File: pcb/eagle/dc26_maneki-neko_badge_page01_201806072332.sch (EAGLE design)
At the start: 49 parts, among them IC1 STM32F030C8T, T1 RK7002BMT116, U2 ESP01, X1 22-23-2021, X2 22-23-2031

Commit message: board outline in, some minor edits to schematic, board ready for component placement
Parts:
- removed LED1, LED2: WS2812B5050, adafruit_2015:WS2812B5050
- removed U$5: PAM2301CAAB330, PAM2301CAAB120:PAM2301CAAB330
- added C10: 1uF/16V/X7R, rcl:C-USC0805
- added H3: TSW-102-07-G-D, con-samtec:TSW-102-07-G-D
- added R26, R27, R28: 10k/5%, rcl:R-US_R0805
- added R29: NO POP, rcl:R-US_R0805
- added U3: ESP01, esp8266modules:ESP01
- C1: value SHORT -> 10uF/16V/X5R
- C3: value 10uF/16V/X5R -> SHORT
- R25: value 10k/5% -> 1k/5%
- U2: value ESP01 -> PAM2301CAAB330; device esp8266modules:ESP01 -> PAM2301CAAB120:PAM2301CAAB330
- U5, U6: value (none) -> MIC2005A-1YM5-TR
- renumbered IC1 to U1, U$1 to D1, U$13 to H1, U$2 to D2, U$3 to U6, U$4 to U5, U$6 to U4, X2 to H2
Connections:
- removed net VCC: C4.1, C5.1, C6.1, H1.1, R21.2, R22.2, U5.VIN, U6.VIN
- new net BOOT0: R28.2, R29.1, U1MCU.BOOT0
- new net I2C1_SCL: H3-4.1, R26.1, U1MCU.PF6
- new net I2C1_SDA: H3-3.1, R27.1, U1MCU.PF7
- net !RESET: now also U1MCU.NRST
- net 3V3: now also C10.1, C2.1, C4.1, C5.1, C6.1, H1.1, H3-1.1, R21.2, R22.2, R26.2, R27.2, R29.2, U1MCU.VDDA, U5.VIN, U6.VIN; no longer C1.1
- net ESP-CH_PD: now also U3.CH_PD; no longer U2.CH_PD
- net ESP-GPIO0: now also U3.GPIO0; no longer U2.GPIO0
- net ESP-GPIO2: now also U3.GPIO2; no longer U2.GPIO2
- net ESP-RST: now also U3.RST; no longer U2.RST
- net ESP-RXD: now also U3.RXD; no longer U2.RXD
- net ESP-TXD: now also U3.TXD; no longer U2.TXD
- net GND: now also C1.2, C10.2, H3-2.1, R28.1, U1MCU.VSSA, U3.GND; no longer C3.2, U$5.GND
- net LED-SEG-A: now also R18.2; no longer R19.2
- net LED-SEG-B: now also R19.2; no longer R18.2
- net LED-SEG-C: now also R15.2; no longer R17.2
- net LED-SEG-E: now also R17.2; no longer R15.2
- net LED-SEG-F: now also R12.2; no longer R14.2
- net LED-SEG-H: now also R14.2; no longer R12.2
- net N$1: now also U2.SW; no longer U$5.SW
- net N$2: now also U2.EN; no longer U$5.EN
- net N$3: now also C3.2, U2.VOUT/FB; no longer C1.2, U$5.VOUT/FB
- net PB0: now also R18.1; no longer R19.1
- net PB1: now also R19.1; no longer R18.1
- net PB2: now also R15.1; no longer R17.1
- net PB4: now also R17.1; no longer R15.1
- net PB5: now also R12.1; no longer R14.1
- net PB7: now also R14.1; no longer R12.1
- net VBAT: now also C1.1, U2.VIN; no longer C2.1, U$5.VIN
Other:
- note added: "BADGELIFE SHITTY ADD-ON HEADER"
- note added: "VOLTAGE REGULATOR"
- moved on the sheet: C1, C2, C3, R10, R12, R14, R15, R16, R17, R18, R19, R20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

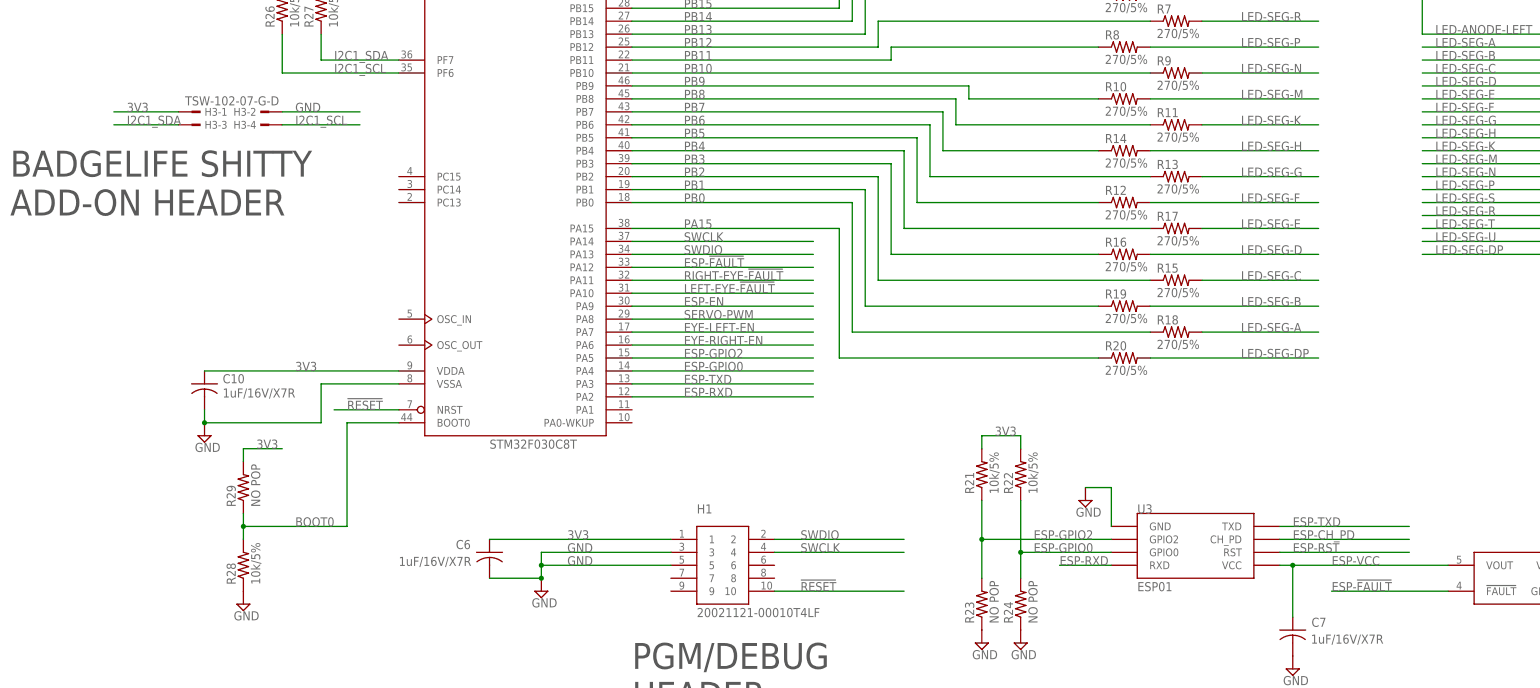
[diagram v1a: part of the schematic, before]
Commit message: more layout. changed out connectors to support a clean 'art' (top) side. shooting for 2 layers, might need to be 4 to avoid a ton of routing time.
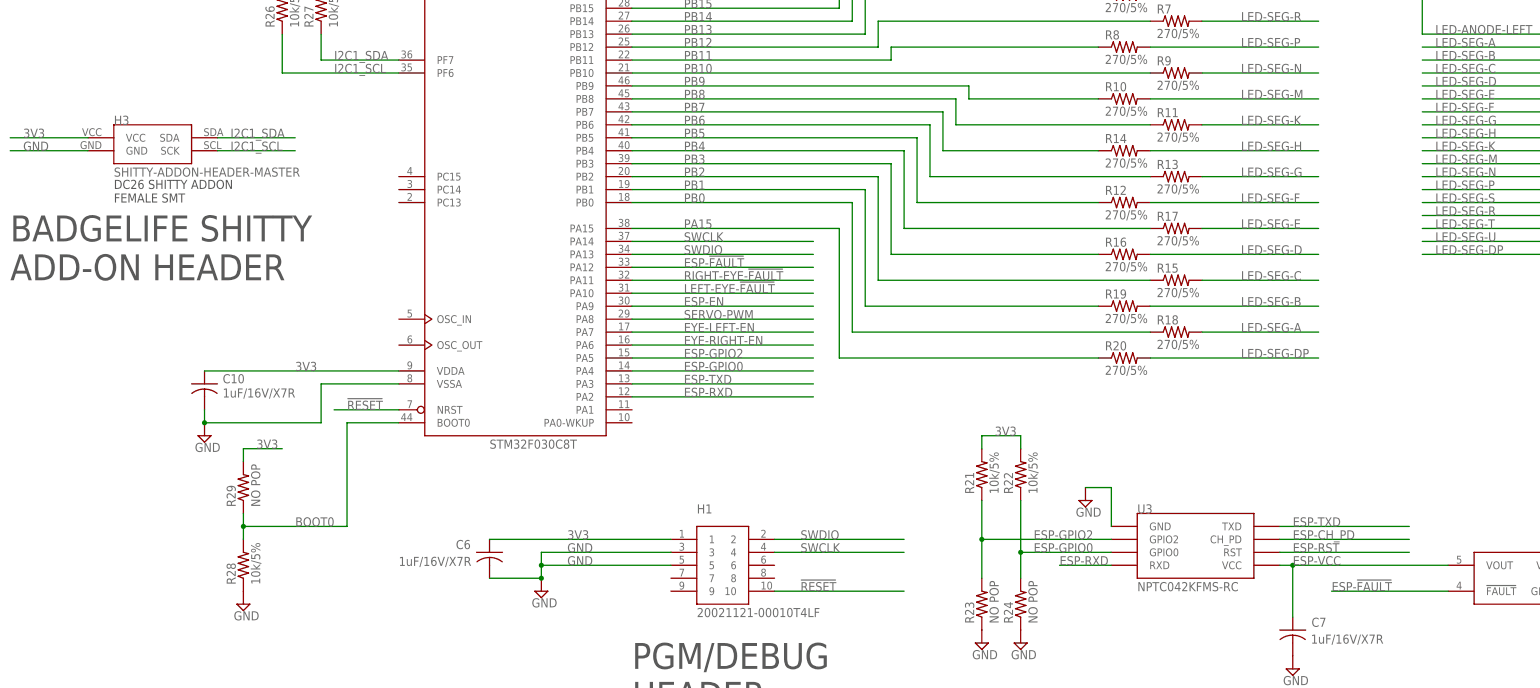
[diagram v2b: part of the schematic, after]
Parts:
- H3: value TSW-102-07-G-D -> SHITTY-ADDON-HEADER-MASTER; device con-samtec:TSW-102-07-G-D -> dc26-shitty-addon:SHITTY-ADDON-HEADER-MASTER
- U3: value ESP01 -> NPTC042KFMS-RC; device esp8266modules:ESP01 -> NPTC042KFMS-RC:NPTC042KFMS-RC
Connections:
- net 3V3: now also H3.VCC; no longer H3-1.1
- net ESP-VCC: now also U3.VCC
- net GND: now also H3.GND; no longer H3-2.1
- net I2C1_SCL: now also H3.SCK; no longer H3-4.1
- net I2C1_SDA: now also H3.SDA; no longer H3-3.1
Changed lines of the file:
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@@
 </classes>
 <parts>
-<part name="U3" library="esp8266modules" deviceset="ESP01" device=""/>
 <part name="U1" library="micro-stm_v3" deviceset="STM32F030C*T" device="" technology="8"/>
 <part name="X1" library="con-molex" library_urn="urn:adsk.eagle:library:165" deviceset="22-23-2021" device=""/>
@@
 <part name="C10" library="rcl" library_urn="urn:adsk.eagle:library:334" deviceset="C-US" device="C0805" package3d_urn="urn:adsk.eagle:package:23617/2" value="1uF/16V/X7R"/>
 <part name="SUPPLY17" library="supply2" library_urn="urn:adsk.eagle:library:372" deviceset="GND" device=""/>
-<part name="H3" library="con-samtec" library_urn="urn:adsk.eagle:library:184" deviceset="TSW-102-*-G" device="-D" technology="07"/>
 <part name="R29" library="rcl" library_urn="urn:adsk.eagle:library:334" deviceset="R-US_" device="R0805" package3d_urn="urn:adsk.eagle:package:23553/2" value="NO POP"/>
 <part name="R28" library="rcl" library_urn="urn:adsk.eagle:library:334" deviceset="R-US_" device="R0805" package3d_urn="urn:adsk.eagle:package:23553/2" value="10k/5%"/>
 <part name="SUPPLY18" library="supply2" library_urn="urn:adsk.eagle:library:372" deviceset="GND" device=""/>
+<part name="H3" library="dc26-shitty-addon" deviceset="SHITTY-ADDON-HEADER-MASTER" device=""/>
+<part name="U3" library="NPTC042KFMS-RC" deviceset="NPTC042KFMS-RC" device=""/>
 </parts>
 <sheets>
@@
 <text x="-121.92" y="40.64" size="5.08" layer="97">PGM/DEBUG
 HEADER</text>
-<text x="-243.84" y="137.16" size="5.08" layer="97">BADGELIFE SHITTY
+<text x="-243.84" y="124.46" size="5.08" layer="97">BADGELIFE SHITTY
 ADD-ON HEADER</text>
 <text x="-134.62" y="238.76" size="5.08" layer="97">VOLTAGE
@@
 </plain>
 <instances>
-<instance part="U3" gate="G$1" x="-10.16" y="68.58"/>
 <instance part="U1" gate="MCU" x="-144.78" y="137.16"/>
 <instance part="X1" gate="-1" x="-172.72" y="226.06" rot="MR0"/>
@@
 </instance>
 <instance part="SUPPLY17" gate="GND" x="-205.74" y="93.98"/>
-<instance part="H3" gate="-1" x="-208.28" y="157.48"/>
-<instance part="H3" gate="-2" x="-193.04" y="157.48" rot="MR0"/>
-<instance part="H3" gate="-3" x="-208.28" y="154.94"/>
-<instance part="H3" gate="-4" x="-193.04" y="154.94" rot="MR0"/>
 <instance part="R29" gate="G$1" x="-198.12" y="83.82" rot="R90"/>
 <instance part="R28" gate="G$1" x="-198.12" y="68.58" rot="R90"/>
 <instance part="SUPPLY18" gate="GND" x="-198.12" y="60.96"/>
+<instance part="H3" gate="G$1" x="-223.52" y="149.86"/>
+<instance part="U3" gate="G$1" x="-10.16" y="68.58"/>
 </instances>
 <busses>
@@
 </segment>
 <segment>
-<pinref part="U3" gate="G$1" pin="GND"/>
 <wire x1="-27.94" y1="76.2" x2="-27.94" y2="83.82" width="0.1524" layer="91"/>
 <pinref part="SUPPLY9" gate="GND" pin="GND"/>
 <wire x1="-27.94" y1="83.82" x2="-33.02" y2="83.82" width="0.1524" layer="91"/>
+<pinref part="U3" gate="G$1" pin="GND"/>
 </segment>
 <segment>
@@
 </segment>
 <segment>
-<pinref part="H3" gate="-2" pin="1"/>
-<wire x1="-190.5" y1="157.48" x2="-175.26" y2="157.48" width="0.1524" layer="91"/>
-<label x="-187.96" y="157.48" size="1.778" layer="95"/>
-</segment>
-<segment>
 <pinref part="R28" gate="G$1" pin="1"/>
 <pinref part="SUPPLY18" gate="GND" pin="GND"/>
+</segment>
+<segment>
+<pinref part="H3" gate="G$1" pin="GND"/>
+<wire x1="-228.6" y1="149.86" x2="-243.84" y2="149.86" width="0.1524" layer="91"/>
+<label x="-241.3" y="149.86" size="1.778" layer="95"/>
 </segment>
 </net>
@@
 </segment>
 <segment>
-<pinref part="H3" gate="-1" pin="1"/>
-<wire x1="-210.82" y1="157.48" x2="-223.52" y2="157.48" width="0.1524" layer="91"/>
-<label x="-220.98" y="157.48" size="1.778" layer="95"/>
-</segment>
-<segment>
 <pinref part="R29" gate="G$1" pin="2"/>
 <wire x1="-198.12" y1="91.44" x2="-198.12" y2="88.9" width="0.1524" layer="91"/>
 <wire x1="-198.12" y1="91.44" x2="-190.5" y2="91.44" width="0.1524" layer="91"/>
 <label x="-195.58" y="91.44" size="1.778" layer="95"/>
+</segment>
+<segment>
+<pinref part="H3" gate="G$1" pin="VCC"/>
+<wire x1="-228.6" y1="152.4" x2="-243.84" y2="152.4" width="0.1524" layer="91"/>
+<label x="-241.3" y="152.4" size="1.778" layer="95"/>
 </segment>
 </net>
@@
 <net name="ESP-TXD" class="0">
 <segment>
-<pinref part="U3" gate="G$1" pin="TXD"/>
 <label x="7.62" y="76.2" size="1.778" layer="95"/>
 <wire x1="5.08" y1="76.2" x2="30.48" y2="76.2" width="0.1524" layer="91"/>
+<pinref part="U3" gate="G$1" pin="TXD"/>
 </segment>
 <segment>
@@
 <net name="ESP-CH_PD" class="0">
 <segment>
-<pinref part="U3" gate="G$1" pin="CH_PD"/>
 <wire x1="5.08" y1="73.66" x2="30.48" y2="73.66" width="0.1524" layer="91"/>
 <label x="7.62" y="73.66" size="1.778" layer="95"/>
+<pinref part="U3" gate="G$1" pin="CH_PD"/>
 </segment>
 </net>
 <net name="ESP-RST" class="0">
 <segment>
-<pinref part="U3" gate="G$1" pin="RST"/>
 <wire x1="5.08" y1="71.12" x2="30.48" y2="71.12" width="0.1524" layer="91"/>
 <label x="7.62" y="71.12" size="1.778" layer="95"/>
+<pinref part="U3" gate="G$1" pin="RST"/>
 </segment>
 </net>
 <net name="ESP-GPIO2" class="0">
 <segment>
-<pinref part="U3" gate="G$1" pin="GPIO2"/>
 <wire x1="-27.94" y1="73.66" x2="-53.34" y2="73.66" width="0.1524" layer="91"/>
 <pinref part="R23" gate="G$1" pin="2"/>
@@
 <junction x="-53.34" y="73.66"/>
 <label x="-43.18" y="73.66" size="1.778" layer="95"/>
+<pinref part="U3" gate="G$1" pin="GPIO2"/>
 </segment>
 <segment>
@@
 <net name="ESP-GPIO0" class="0">
 <segment>
-<pinref part="U3" gate="G$1" pin="GPIO0"/>
 <wire x1="-27.94" y1="71.12" x2="-45.72" y2="71.12" width="0.1524" layer="91"/>
 <pinref part="R24" gate="G$1" pin="2"/>
@@
 <wire x1="-45.72" y1="71.12" x2="-45.72" y2="81.28" width="0.1524" layer="91"/>
 <label x="-43.18" y="71.12" size="1.778" layer="95"/>
+<pinref part="U3" gate="G$1" pin="GPIO0"/>
 </segment>
 <segment>
@@
 <net name="ESP-RXD" class="0">
 <segment>
-<pinref part="U3" gate="G$1" pin="RXD"/>
 <wire x1="-27.94" y1="68.58" x2="-38.1" y2="68.58" width="0.1524" layer="91"/>
 <label x="-38.1" y="68.58" size="1.778" layer="95"/>
+<pinref part="U3" gate="G$1" pin="RXD"/>
 </segment>
 <segment>
@@
 <wire x1="-121.92" y1="101.6" x2="-86.36" y2="101.6" width="0.1524" layer="91"/>
 <label x="-111.76" y="101.6" size="1.778" layer="95"/>
-</segment>
-</net>
-<net name="ESP-VCC" class="0">
-<segment>
-<pinref part="U4" gate="G$1" pin="VOUT"/>
-<wire x1="38.1" y1="68.58" x2="7.62" y2="68.58" width="0.1524" layer="91"/>
-<pinref part="C7" gate="G$1" pin="1"/>
-<wire x1="7.62" y1="68.58" x2="5.08" y2="68.58" width="0.1524" layer="91"/>
-<wire x1="7.62" y1="58.42" x2="7.62" y2="68.58" width="0.1524" layer="91"/>
-<junction x="7.62" y="68.58"/>
-<label x="15.24" y="68.58" size="1.778" layer="95"/>
 </segment>
 </net>
@@
 </segment>
 <segment>
-<pinref part="H3" gate="-4" pin="1"/>
-<wire x1="-190.5" y1="154.94" x2="-175.26" y2="154.94" width="0.1524" layer="91"/>
-<label x="-187.96" y="154.94" size="1.778" layer="95"/>
+<pinref part="H3" gate="G$1" pin="SCK"/>
+<wire x1="-203.2" y1="149.86" x2="-187.96" y2="149.86" width="0.1524" layer="91"/>
+<label x="-200.66" y="149.86" size="1.778" layer="95"/>
 </segment>
 </net>
@@
 </segment>
 <segment>
-<pinref part="H3" gate="-3" pin="1"/>
-<wire x1="-210.82" y1="154.94" x2="-223.52" y2="154.94" width="0.1524" layer="91"/>
-<label x="-220.98" y="154.94" size="1.778" layer="95"/>
+<pinref part="H3" gate="G$1" pin="SDA"/>
+<wire x1="-203.2" y1="152.4" x2="-187.96" y2="152.4" width="0.1524" layer="91"/>
+<label x="-200.66" y="152.4" size="1.778" layer="95"/>
 </segment>
 </net>
@@
 </segment>
 </net>
+<net name="ESP-VCC" class="0">
+<segment>
+<pinref part="U4" gate="G$1" pin="VOUT"/>
+<wire x1="5.08" y1="68.58" x2="7.62" y2="68.58" width="0.1524" layer="91"/>
+<pinref part="C7" gate="G$1" pin="1"/>
+<wire x1="7.62" y1="68.58" x2="38.1" y2="68.58" width="0.1524" layer="91"/>
+<wire x1="7.62" y1="58.42" x2="7.62" y2="68.58" width="0.1524" layer="91"/>
+<junction x="7.62" y="68.58"/>
+<label x="7.62" y="68.58" size="1.778" layer="95"/>
+<pinref part="U3" gate="G$1" pin="VCC"/>
+</segment>
+</net>

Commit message: completely regretting my decision to use eagle
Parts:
- added C11, C12: 1uF/16V/X7R, rcl:C-USC0805
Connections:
- net 3V3: now also C11.1, C12.1, U1PWR.VDD@1, U1PWR.VDD@2, U1PWR.VDD@3
- net GND: now also C11.2, C12.2, U1PWR.VSS@1, U1PWR.VSS@2
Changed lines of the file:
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@@
 <part name="H3" library="dc26-shitty-addon" deviceset="SHITTY-ADDON-HEADER-MASTER" device=""/>
 <part name="U3" library="NPTC042KFMS-RC" deviceset="NPTC042KFMS-RC" device=""/>
+<part name="C11" library="rcl" library_urn="urn:adsk.eagle:library:334" deviceset="C-US" device="C0805" package3d_urn="urn:adsk.eagle:package:23617/2" value="1uF/16V/X7R"/>
+<part name="C12" library="rcl" library_urn="urn:adsk.eagle:library:334" deviceset="C-US" device="C0805" package3d_urn="urn:adsk.eagle:package:23617/2" value="1uF/16V/X7R"/>
+<part name="SUPPLY19" library="supply2" library_urn="urn:adsk.eagle:library:372" deviceset="GND" device=""/>
+<part name="SUPPLY20" library="supply2" library_urn="urn:adsk.eagle:library:372" deviceset="GND" device=""/>
 </parts>
 <sheets>
@@
 </plain>
 <instances>
-<instance part="U1" gate="MCU" x="-144.78" y="137.16"/>
+<instance part="U1" gate="MCU" x="-144.78" y="137.16" smashed="yes">
+<attribute name="NAME" x="-149.86" y="182.88" size="1.778" layer="95"/>
+<attribute name="VALUE" x="-149.86" y="91.44" size="1.778" layer="96"/>
+</instance>
 <instance part="X1" gate="-1" x="-172.72" y="226.06" rot="MR0"/>
 <instance part="X1" gate="-2" x="-172.72" y="223.52" rot="MR0"/>
@@
 <instance part="H3" gate="G$1" x="-223.52" y="149.86"/>
 <instance part="U3" gate="G$1" x="-10.16" y="68.58"/>
+<instance part="U1" gate="PWR" x="-147.32" y="190.5" rot="R270"/>
+<instance part="C11" gate="G$1" x="-88.9" y="195.58" smashed="yes" rot="MR0">
+<attribute name="NAME" x="-85.344" y="197.485" size="1.778" layer="95" rot="MR180"/>
+<attribute name="VALUE" x="-85.344" y="194.691" size="1.778" layer="96" rot="MR180"/>
+</instance>
+<instance part="C12" gate="G$1" x="-96.52" y="195.58" smashed="yes">
+<attribute name="NAME" x="-100.076" y="197.485" size="1.778" layer="95" rot="R180"/>
+<attribute name="VALUE" x="-100.076" y="194.691" size="1.778" layer="96" rot="R180"/>
+</instance>
+<instance part="SUPPLY19" gate="GND" x="-167.64" y="182.88"/>
+<instance part="SUPPLY20" gate="GND" x="-96.52" y="185.42"/>
 </instances>
 <busses>
@@
 <label x="-241.3" y="149.86" size="1.778" layer="95"/>
 </segment>
+<segment>
+<pinref part="SUPPLY19" gate="GND" pin="GND"/>
+<pinref part="U1" gate="PWR" pin="VSS@1"/>
+<wire x1="-167.64" y1="185.42" x2="-167.64" y2="187.96" width="0.1524" layer="91"/>
+<wire x1="-167.64" y1="187.96" x2="-167.64" y2="193.04" width="0.1524" layer="91"/>
+<wire x1="-167.64" y1="193.04" x2="-165.1" y2="193.04" width="0.1524" layer="91"/>
+<pinref part="U1" gate="PWR" pin="VSS@2"/>
+<wire x1="-165.1" y1="187.96" x2="-167.64" y2="187.96" width="0.1524" layer="91"/>
+<junction x="-167.64" y="187.96"/>
+</segment>
+<segment>
+<pinref part="C12" gate="G$1" pin="2"/>
+<pinref part="SUPPLY20" gate="GND" pin="GND"/>
+<wire x1="-96.52" y1="190.5" x2="-96.52" y2="187.96" width="0.1524" layer="91"/>
+<pinref part="C11" gate="G$1" pin="2"/>
+<wire x1="-88.9" y1="190.5" x2="-88.9" y2="187.96" width="0.1524" layer="91"/>
+<wire x1="-88.9" y1="187.96" x2="-96.52" y2="187.96" width="0.1524" layer="91"/>
+<junction x="-96.52" y="187.96"/>
+</segment>
 </net>
 <net name="VBAT" class="0">
@@
 <label x="-241.3" y="152.4" size="1.778" layer="95"/>
 </segment>
+<segment>
+<pinref part="U1" gate="PWR" pin="VDD@3"/>
+<wire x1="-129.54" y1="185.42" x2="-127" y2="185.42" width="0.1524" layer="91"/>
+<wire x1="-127" y1="185.42" x2="-127" y2="190.5" width="0.1524" layer="91"/>
+<pinref part="U1" gate="PWR" pin="VDD@1"/>
+<wire x1="-127" y1="190.5" x2="-127" y2="195.58" width="0.1524" layer="91"/>
+<wire x1="-127" y1="195.58" x2="-129.54" y2="195.58" width="0.1524" layer="91"/>
+<pinref part="U1" gate="PWR" pin="VDD@2"/>
+<wire x1="-129.54" y1="190.5" x2="-127" y2="190.5" width="0.1524" layer="91"/>
+<junction x="-127" y="190.5"/>
+<wire x1="-127" y1="195.58" x2="-116.84" y2="195.58" width="0.1524" layer="91"/>
+<label x="-124.46" y="195.58" size="1.778" layer="95"/>
+<junction x="-127" y="195.58"/>
+</segment>
+<segment>
+<pinref part="C12" gate="G$1" pin="1"/>
+<wire x1="-96.52" y1="198.12" x2="-96.52" y2="200.66" width="0.1524" layer="91"/>
+<wire x1="-96.52" y1="200.66" x2="-104.14" y2="200.66" width="0.1524" layer="91"/>
+<pinref part="C11" gate="G$1" pin="1"/>
+<wire x1="-88.9" y1="198.12" x2="-88.9" y2="200.66" width="0.1524" layer="91"/>
+<wire x1="-88.9" y1="200.66" x2="-96.52" y2="200.66" width="0.1524" layer="91"/>
+<junction x="-96.52" y="200.66"/>
+<label x="-104.14" y="200.66" size="1.778" layer="95"/>
+</segment>
 </net>

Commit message: mini commit before taking a shower and letting autorouter mess around
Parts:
- removed X1: 22-23-2021, con-molex:22-23-2021
- added U$1: BATTPADS-SMT, battery_pads:BATTPADS-SMT
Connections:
- net GND: now also U$1.2; no longer X1-2.S
- net VBAT: now also U$1.1; no longer X1-1.S
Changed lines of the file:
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@@
 <parts>
 <part name="U1" library="micro-stm_v3" deviceset="STM32F030C*T" device="" technology="8"/>
-<part name="X1" library="con-molex" library_urn="urn:adsk.eagle:library:165" deviceset="22-23-2021" device=""/>
 <part name="SUPPLY1" library="supply2" library_urn="urn:adsk.eagle:library:372" deviceset="GND" device=""/>
 <part name="L1" library="passives" deviceset="CIG22L4R7MNE" device=""/>
@@
 <part name="SUPPLY19" library="supply2" library_urn="urn:adsk.eagle:library:372" deviceset="GND" device=""/>
 <part name="SUPPLY20" library="supply2" library_urn="urn:adsk.eagle:library:372" deviceset="GND" device=""/>
+<part name="U$1" library="battery_pads" deviceset="BATTPADS-SMT" device=""/>
 </parts>
 <sheets>
@@
 <attribute name="VALUE" x="-149.86" y="91.44" size="1.778" layer="96"/>
 </instance>
-<instance part="X1" gate="-1" x="-172.72" y="226.06" rot="MR0"/>
-<instance part="X1" gate="-2" x="-172.72" y="223.52" rot="MR0"/>
 <instance part="SUPPLY1" gate="GND" x="-165.1" y="220.98"/>
 <instance part="L1" gate="G$1" x="-66.04" y="223.52" smashed="yes" rot="R90">
@@
 <instance part="SUPPLY19" gate="GND" x="-167.64" y="182.88"/>
 <instance part="SUPPLY20" gate="GND" x="-96.52" y="185.42"/>
+<instance part="U$1" gate="G$1" x="-175.26" y="226.06" rot="MR0"/>
 </instances>
 <busses>
@@
 <net name="GND" class="0">
 <segment>
-<pinref part="X1" gate="-2" pin="S"/>
 <pinref part="SUPPLY1" gate="GND" pin="GND"/>
 <wire x1="-170.18" y1="223.52" x2="-165.1" y2="223.52" width="0.1524" layer="91"/>
+<pinref part="U$1" gate="G$1" pin="2"/>
 </segment>
 <segment>
@@
 <net name="VBAT" class="0">
 <segment>
-<pinref part="X1" gate="-1" pin="S"/>
 <label x="-162.56" y="226.06" size="1.778" layer="95"/>
 <pinref part="C1" gate="G$1" pin="1"/>
@@
 <junction x="-134.62" y="220.98"/>
 <pinref part="U2" gate="G$1" pin="VIN"/>
-</segment>
-<segment>
+<pinref part="U$1" gate="G$1" pin="1"/>
+</segment>
+<segment>
